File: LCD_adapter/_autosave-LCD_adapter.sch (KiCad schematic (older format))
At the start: 5 parts, among them J1 Conn_01x15_Male, J2 Conn_01x15_Male, U1 RC1602A

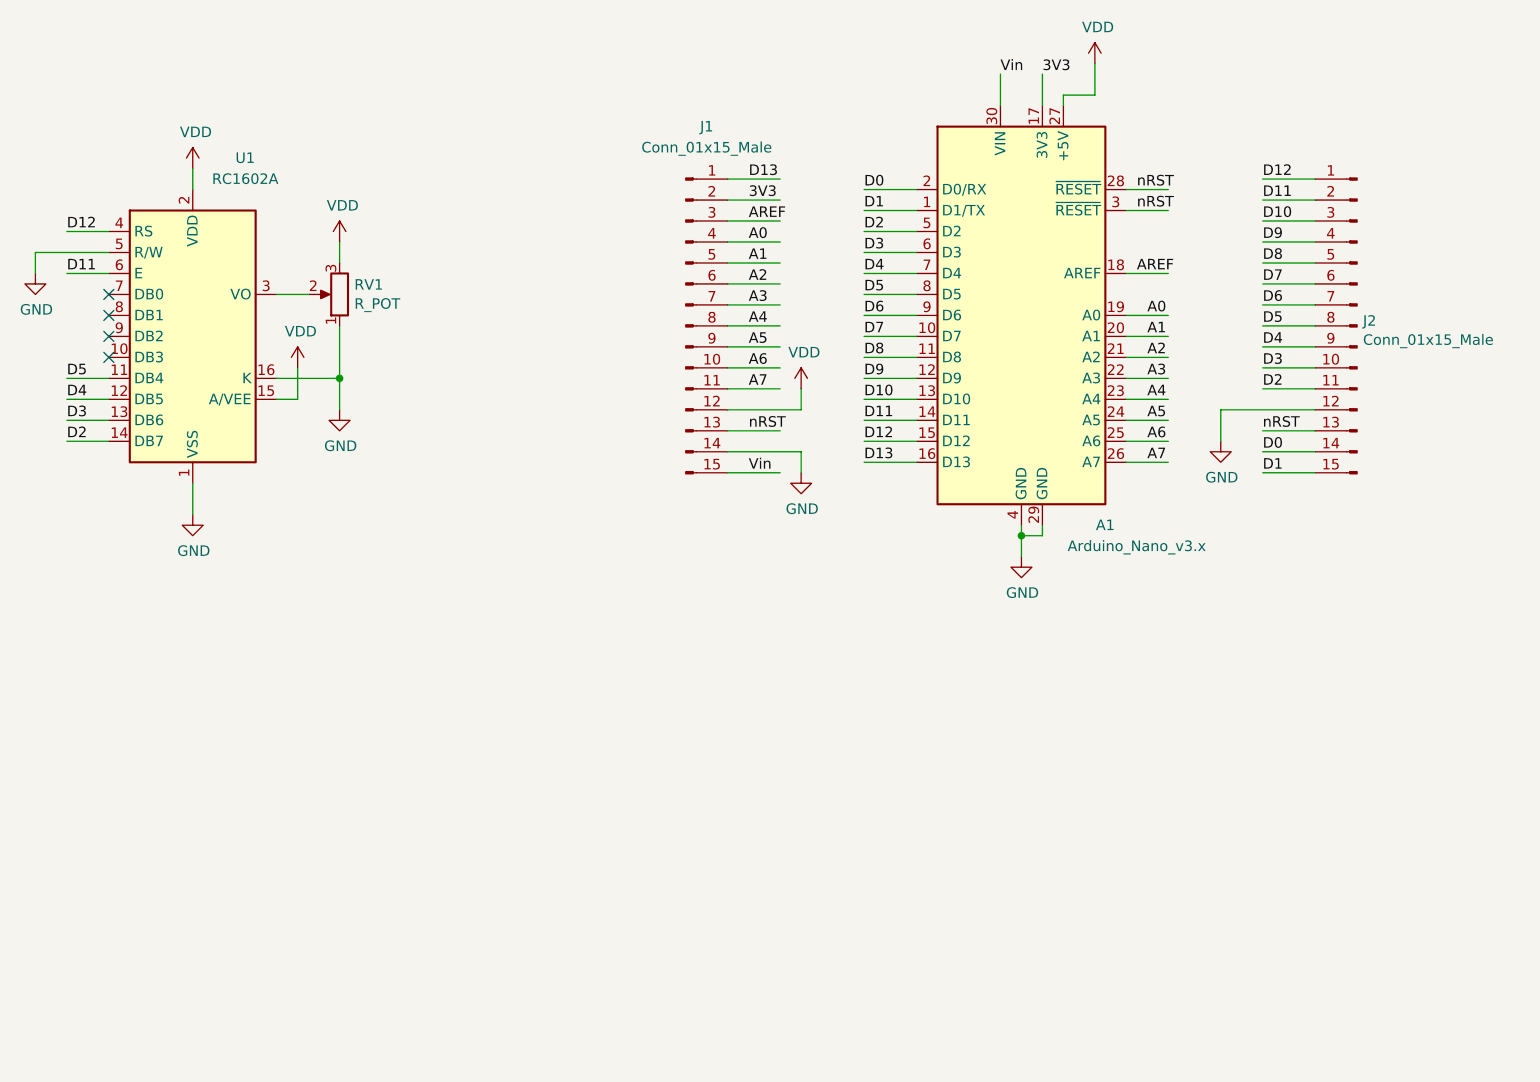
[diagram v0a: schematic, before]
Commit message: bluetooth module v0 - updated to include the bluetooth module and buttons for control
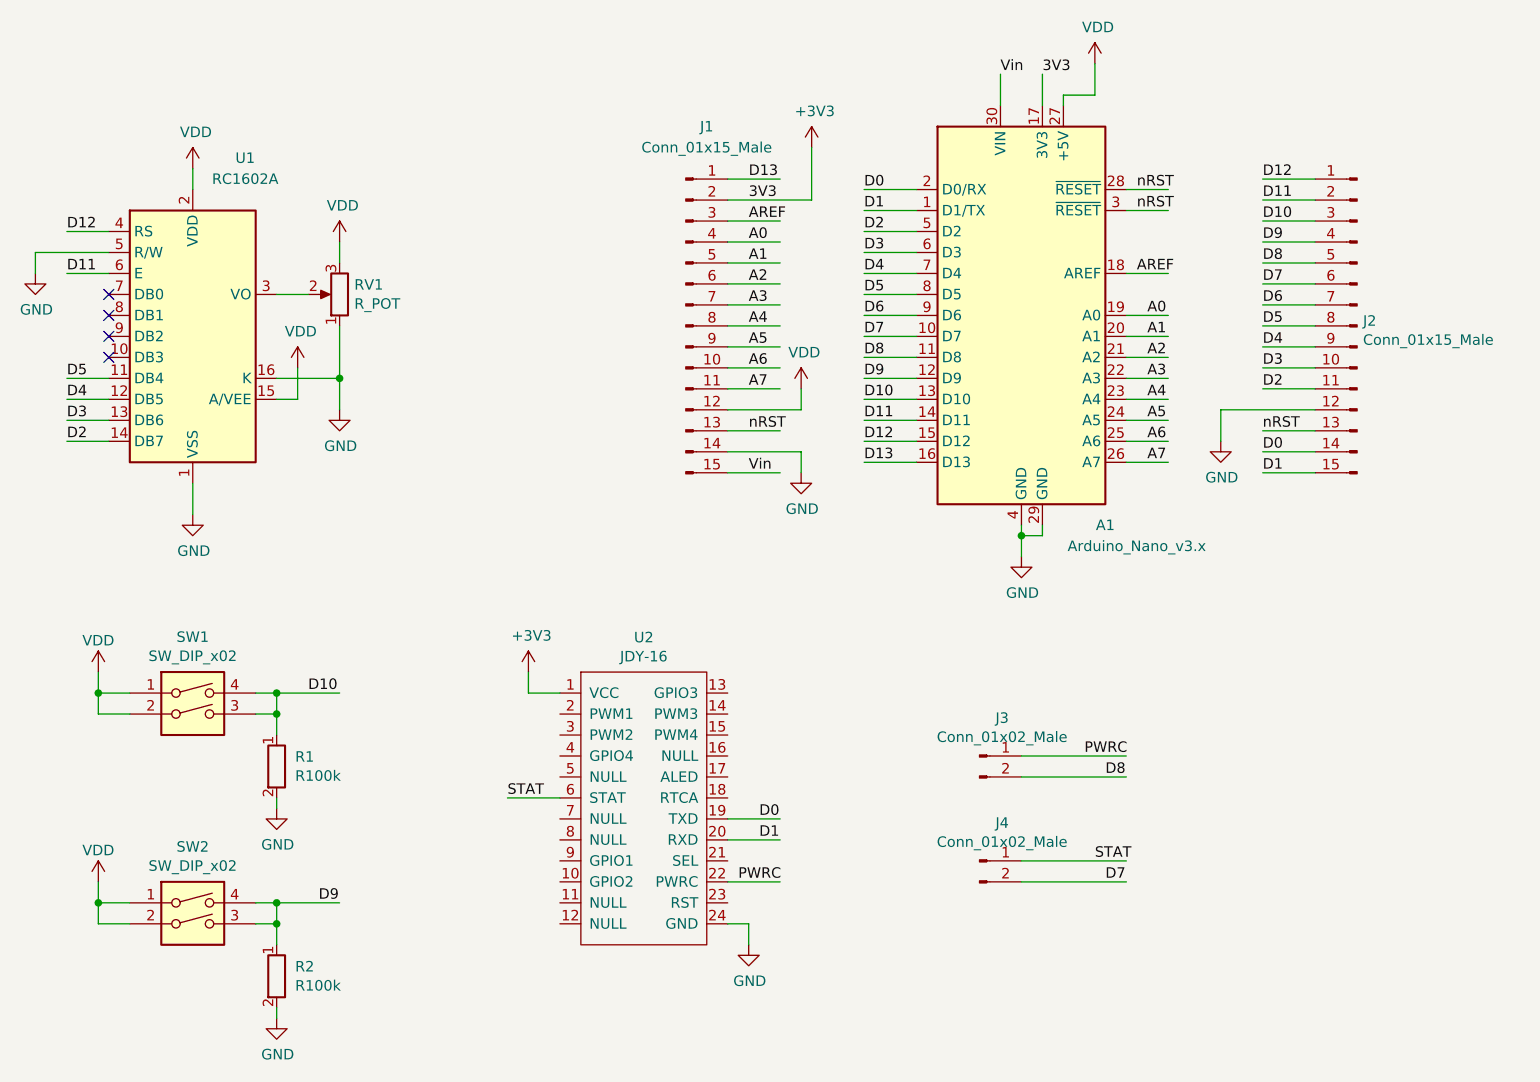
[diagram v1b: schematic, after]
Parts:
- added J3, J4: Conn_01x02_Male, Connector_PinHeader_2.54mm:PinHeader_1x02_P2.54mm_Vertical, symbol Connector:Conn_01x02_Male
- added R1, R2: R100k, Resistor_THT:R_Axial_DIN0207_L6.3mm_D2.5mm_P7.62mm_Horizontal, symbol resistors:R100k
- added SW1, SW2: SW_DIP_x02, brad_footprints:SW_PUSH_6mm_H9.5mm, symbol Switch:SW_DIP_x02
- added U2: JDY-16, brad_footprints:JDY-16, symbol brad_lib:JDY-16
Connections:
- net labels added: +3V3, PWRC, STAT
- wire segments 84 -> 117
